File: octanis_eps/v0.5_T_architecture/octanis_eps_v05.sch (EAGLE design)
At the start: 141 parts, among them IC1 OPA2333DGK, Q3 32.768kHz, Q4 BSS123, U1 BQ24650_RVA_16, U10 CSD16327Q3_DQG_8, U13 CSD16327Q3_DQG_8, U14 CSD16327Q3_DQG_8, U2 TPS630250, U3 TPS630250, U4 TPS630250, U5 TPS2022D, U6 TPS61232, U7 CSD16327Q3_DQG_8, U8 MSP430G2544, U9 CSD16327Q3_DQG_8

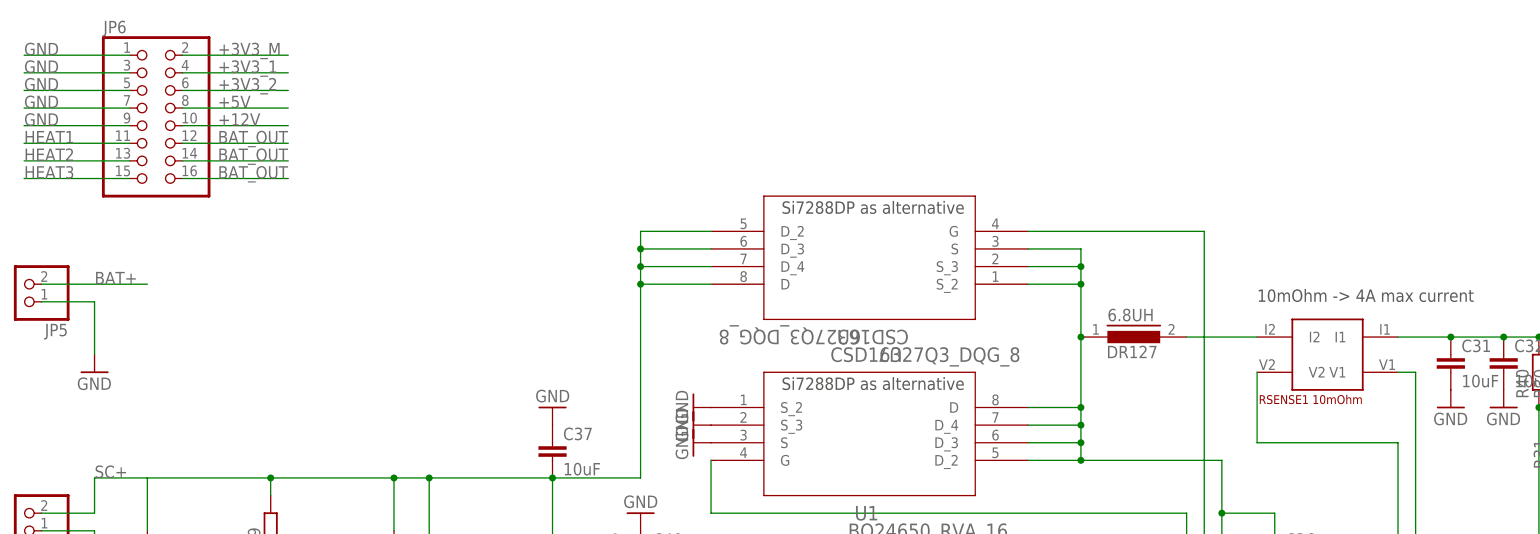
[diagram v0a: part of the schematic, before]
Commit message: Arranged parts for EPS v05
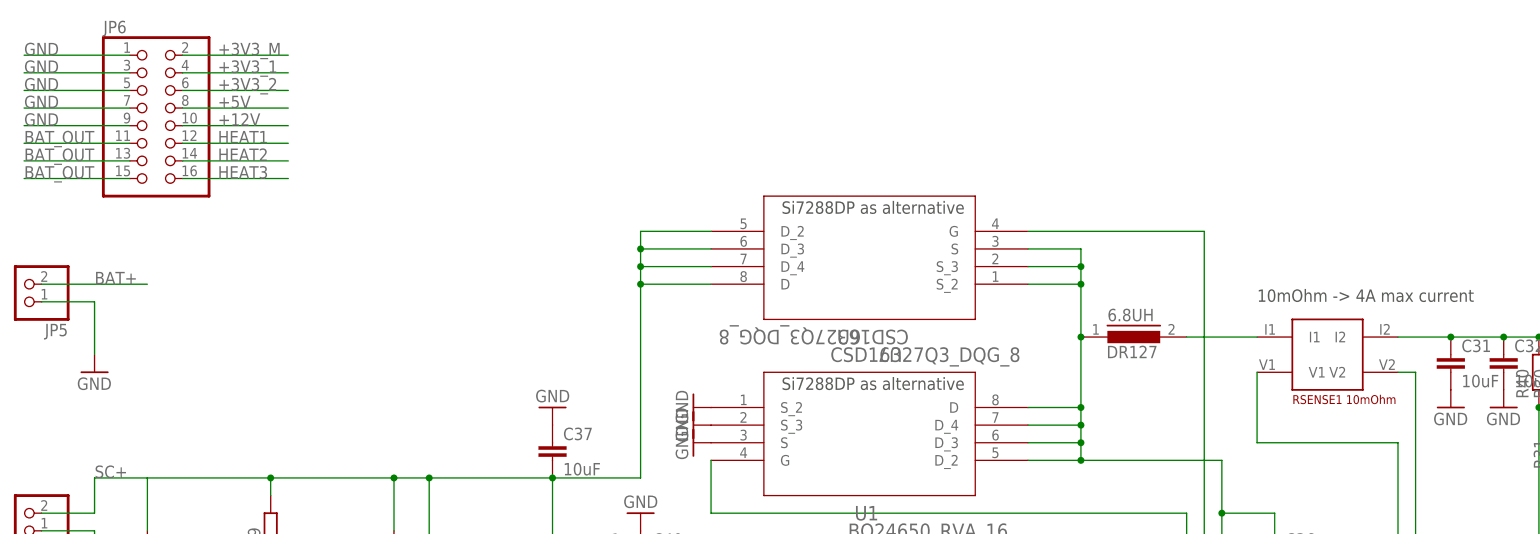
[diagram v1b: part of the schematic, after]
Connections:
- removed net N$79: 6.8UH.2, R_SENSE2.I2
- new net N$4: 6.8UH.2, R_SENSE2.I1
- net BAT_OUT: now also JP6.11, JP6.13, JP6.15; no longer JP6.12, JP6.14, JP6.16
- net HEAT1: now also JP6.12; no longer JP6.11
- net HEAT2: now also JP6.14; no longer JP6.13
- net HEAT3: now also JP6.16; no longer JP6.15
- net N$77: now also R_SENSE2.V1; no longer R_SENSE2.V2
- net N$78: now also R_SENSE2.V2; no longer R_SENSE2.V1
- net SC_OUT: now also R_SENSE2.I2; no longer R_SENSE2.I1
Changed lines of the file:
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@@
 <attribute name="VALUE" x="192.024" y="71.501" size="1.778" layer="96"/>
 </instance>
-<instance part="R_SENSE2" gate="G$1" x="193.04" y="101.6" rot="R180"/>
+<instance part="R_SENSE2" gate="G$1" x="203.2" y="101.6" rot="MR180"/>
 <instance part="GND57" gate="1" x="223.52" y="93.98"/>
 <instance part="GND58" gate="1" x="215.9" y="93.98"/>
@@
 </segment>
 <segment>
-<pinref part="JP6" gate="A" pin="15"/>
-<wire x1="25.4" y1="127" x2="10.16" y2="127" width="0.1524" layer="91"/>
-<label x="10.16" y="127" size="1.778" layer="95"/>
+<pinref part="JP6" gate="A" pin="16"/>
+<wire x1="33.02" y1="127" x2="48.26" y2="127" width="0.1524" layer="91"/>
+<label x="38.1" y="127" size="1.778" layer="95"/>
 </segment>
 </net>
@@
 </segment>
 <segment>
-<pinref part="JP6" gate="A" pin="13"/>
-<wire x1="25.4" y1="129.54" x2="10.16" y2="129.54" width="0.1524" layer="91"/>
-<label x="10.16" y="129.54" size="1.778" layer="95"/>
+<pinref part="JP6" gate="A" pin="14"/>
+<wire x1="33.02" y1="129.54" x2="48.26" y2="129.54" width="0.1524" layer="91"/>
+<label x="38.1" y="129.54" size="1.778" layer="95"/>
 </segment>
 </net>
@@
 </segment>
 <segment>
-<pinref part="JP6" gate="A" pin="11"/>
-<wire x1="25.4" y1="132.08" x2="10.16" y2="132.08" width="0.1524" layer="91"/>
-<label x="10.16" y="132.08" size="1.778" layer="95"/>
+<pinref part="JP6" gate="A" pin="12"/>
+<wire x1="33.02" y1="132.08" x2="48.26" y2="132.08" width="0.1524" layer="91"/>
+<label x="38.1" y="132.08" size="1.778" layer="95"/>
 </segment>
 </net>
@@
 <wire x1="182.88" y1="53.34" x2="208.28" y2="53.34" width="0.1524" layer="91"/>
 <wire x1="208.28" y1="53.34" x2="208.28" y2="88.9" width="0.1524" layer="91"/>
-<pinref part="R_SENSE2" gate="G$1" pin="V2"/>
 <wire x1="208.28" y1="88.9" x2="187.96" y2="88.9" width="0.1524" layer="91"/>
+<pinref part="R_SENSE2" gate="G$1" pin="V1"/>
 <wire x1="187.96" y1="88.9" x2="187.96" y2="99.06" width="0.1524" layer="91"/>
 </segment>
@@
 <wire x1="177.8" y1="45.72" x2="182.88" y2="45.72" width="0.1524" layer="91"/>
 <junction x="182.88" y="45.72"/>
-<pinref part="R_SENSE2" gate="G$1" pin="V1"/>
+<wire x1="210.82" y1="45.72" x2="182.88" y2="45.72" width="0.1524" layer="91"/>
+<pinref part="R_SENSE2" gate="G$1" pin="V2"/>
 <wire x1="208.28" y1="99.06" x2="210.82" y2="99.06" width="0.1524" layer="91"/>
 <wire x1="210.82" y1="99.06" x2="210.82" y2="45.72" width="0.1524" layer="91"/>
-<wire x1="210.82" y1="45.72" x2="182.88" y2="45.72" width="0.1524" layer="91"/>
 </segment>
 </net>
@@
 <wire x1="238.76" y1="101.6" x2="238.76" y2="104.14" width="0.1524" layer="91"/>
 <wire x1="238.76" y1="104.14" x2="231.14" y2="104.14" width="0.1524" layer="91"/>
-<pinref part="R_SENSE2" gate="G$1" pin="I1"/>
-<wire x1="208.28" y1="104.14" x2="215.9" y2="104.14" width="0.1524" layer="91"/>
 <pinref part="C31" gate="G$1" pin="1"/>
-<junction x="215.9" y="104.14"/>
 <wire x1="215.9" y1="104.14" x2="223.52" y2="104.14" width="0.1524" layer="91"/>
 <pinref part="C32" gate="G$1" pin="1"/>
@@
 <junction x="238.76" y="104.14"/>
 <label x="238.76" y="104.14" size="1.778" layer="95"/>
+<pinref part="R_SENSE2" gate="G$1" pin="I2"/>
+<wire x1="208.28" y1="104.14" x2="215.9" y2="104.14" width="0.1524" layer="91"/>
+<junction x="215.9" y="104.14"/>
 </segment>
 <segment>
@@
 <junction x="190.5" y="66.04"/>
 <pinref part="D1" gate="G$1" pin="CC"/>
-</segment>
-</net>
-<net name="N$79" class="0">
-<segment>
-<pinref part="6.8UH" gate="G$1" pin="2"/>
-<pinref part="R_SENSE2" gate="G$1" pin="I2"/>
-<wire x1="187.96" y1="104.14" x2="177.8" y2="104.14" width="0.1524" layer="91"/>
 </segment>
 </net>
@@
 </segment>
 <segment>
-<pinref part="JP6" gate="A" pin="12"/>
-<wire x1="33.02" y1="132.08" x2="48.26" y2="132.08" width="0.1524" layer="91"/>
-<label x="38.1" y="132.08" size="1.778" layer="95"/>
-</segment>
-<segment>
-<pinref part="JP6" gate="A" pin="14"/>
-<wire x1="33.02" y1="129.54" x2="48.26" y2="129.54" width="0.1524" layer="91"/>
-<label x="38.1" y="129.54" size="1.778" layer="95"/>
-</segment>
-<segment>
-<pinref part="JP6" gate="A" pin="16"/>
-<wire x1="33.02" y1="127" x2="48.26" y2="127" width="0.1524" layer="91"/>
-<label x="38.1" y="127" size="1.778" layer="95"/>
+<pinref part="JP6" gate="A" pin="11"/>
+<wire x1="25.4" y1="132.08" x2="10.16" y2="132.08" width="0.1524" layer="91"/>
+<label x="10.16" y="132.08" size="1.778" layer="95"/>
+</segment>
+<segment>
+<pinref part="JP6" gate="A" pin="13"/>
+<wire x1="25.4" y1="129.54" x2="10.16" y2="129.54" width="0.1524" layer="91"/>
+<label x="10.16" y="129.54" size="1.778" layer="95"/>
+</segment>
+<segment>
+<pinref part="JP6" gate="A" pin="15"/>
+<wire x1="25.4" y1="127" x2="10.16" y2="127" width="0.1524" layer="91"/>
+<label x="10.16" y="127" size="1.778" layer="95"/>
 </segment>
 </net>
@@
 </segment>
 </net>
+<net name="N$4" class="0">
+<segment>
+<pinref part="R_SENSE2" gate="G$1" pin="I1"/>
+<pinref part="6.8UH" gate="G$1" pin="2"/>
+<wire x1="187.96" y1="104.14" x2="177.8" y2="104.14" width="0.1524" layer="91"/>
+</segment>
+</net>

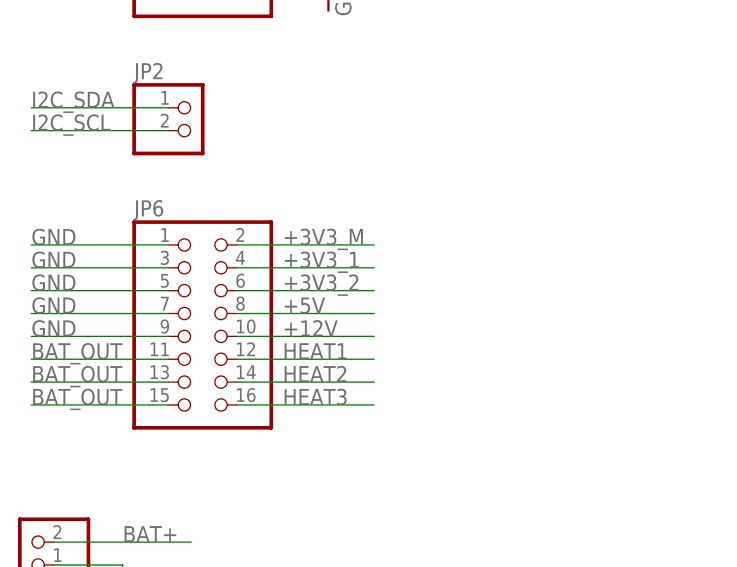
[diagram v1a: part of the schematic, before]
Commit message: Routed 3.3V, 5V and Solar Cell stepdown
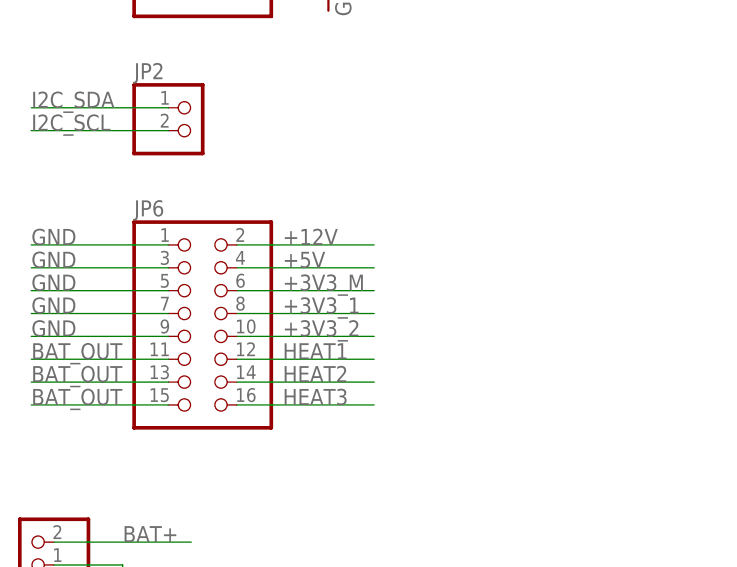
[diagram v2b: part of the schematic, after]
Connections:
- net +12V: now also JP6.2; no longer JP6.10
- net +3V3_1: now also JP6.8; no longer JP6.4
- net +3V3_2: now also JP6.10; no longer JP6.6
- net +3V3_M: now also JP6.6; no longer JP6.2
- net +5V: now also JP6.4; no longer JP6.8
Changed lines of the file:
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@@
 </segment>
 <segment>
-<pinref part="JP6" gate="A" pin="2"/>
-<wire x1="33.02" y1="144.78" x2="48.26" y2="144.78" width="0.1524" layer="91"/>
-<label x="38.1" y="144.78" size="1.778" layer="95"/>
+<pinref part="JP6" gate="A" pin="6"/>
+<wire x1="33.02" y1="139.7" x2="48.26" y2="139.7" width="0.1524" layer="91"/>
+<label x="38.1" y="139.7" size="1.778" layer="95"/>
 </segment>
 </net>
@@
 </segment>
 <segment>
-<pinref part="JP6" gate="A" pin="4"/>
-<wire x1="33.02" y1="142.24" x2="48.26" y2="142.24" width="0.1524" layer="91"/>
-<label x="38.1" y="142.24" size="1.778" layer="95"/>
+<pinref part="JP6" gate="A" pin="8"/>
+<wire x1="33.02" y1="137.16" x2="48.26" y2="137.16" width="0.1524" layer="91"/>
+<label x="38.1" y="137.16" size="1.778" layer="95"/>
 </segment>
 </net>
@@
 </segment>
 <segment>
-<pinref part="JP6" gate="A" pin="6"/>
-<wire x1="33.02" y1="139.7" x2="48.26" y2="139.7" width="0.1524" layer="91"/>
-<label x="38.1" y="139.7" size="1.778" layer="95"/>
+<pinref part="JP6" gate="A" pin="10"/>
+<wire x1="33.02" y1="134.62" x2="48.26" y2="134.62" width="0.1524" layer="91"/>
+<label x="38.1" y="134.62" size="1.778" layer="95"/>
 </segment>
 </net>
@@
 </segment>
 <segment>
-<pinref part="JP6" gate="A" pin="10"/>
-<wire x1="33.02" y1="134.62" x2="48.26" y2="134.62" width="0.1524" layer="91"/>
-<label x="38.1" y="134.62" size="1.778" layer="95"/>
+<pinref part="JP6" gate="A" pin="2"/>
+<wire x1="33.02" y1="144.78" x2="48.26" y2="144.78" width="0.1524" layer="91"/>
+<label x="38.1" y="144.78" size="1.778" layer="95"/>
 </segment>
 </net>
@@
 </segment>
 <segment>
-<pinref part="JP6" gate="A" pin="8"/>
-<wire x1="33.02" y1="137.16" x2="48.26" y2="137.16" width="0.1524" layer="91"/>
-<label x="38.1" y="137.16" size="1.778" layer="95"/>
-</segment>
-</net>
+<pinref part="JP6" gate="A" pin="4"/>
+<wire x1="33.02" y1="142.24" x2="48.26" y2="142.24" width="0.1524" layer="91"/>
+<label x="38.1" y="142.24" size="1.778" layer="95"/>
+</segment>
+</net>

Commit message: EPS v05 routing complete
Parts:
- U1: device texasinstruments:BQ24650_RVA_16 -> octanis_eps_v05:BQ24650_RVA_16
- U2, U3, U4: value TPS630250 -> Value; device texasinstruments:TPS630250RNCR -> octanis_eps_v05:TPS630250RNCR
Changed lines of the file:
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@@
 <classes>
 <class number="0" name="default" width="0" drill="0">
-<clearance class="0" value="0.205"/>
+<clearance class="0" value="0.1524"/>
 </class>
 <class number="1" name="power" width="0.2032" drill="0.3048">
@@
 </classes>
 <parts>
-<part name="U1" library="texasinstruments" deviceset="BQ24650_RVA_16" device=""/>
-<part name="U2" library="texasinstruments" deviceset="TPS630250RNCR" device="" value="TPS630250"/>
+<part name="U1" library="octanis_eps_v05" deviceset="BQ24650_RVA_16" device=""/>
+<part name="U2" library="octanis_eps_v05" deviceset="TPS630250RNCR" device="" value="Value"/>
 <part name="U5" library="Octanis1_EPS" deviceset="TPS2022D" device=""/>
 <part name="U8" library="Octanis1_EPS" deviceset="MSP430G2544" device=""/>
@@
 <part name="GND6" library="supply1" deviceset="GND" device=""/>
 <part name="GND7" library="supply1" deviceset="GND" device=""/>
-<part name="U3" library="texasinstruments" deviceset="TPS630250RNCR" device="" value="TPS630250"/>
+<part name="U3" library="octanis_eps_v05" deviceset="TPS630250RNCR" device="" value="Value"/>
 <part name="C4" library="resistor" deviceset="C-EU" device="C0805" value="10uF"/>
 <part name="C5" library="resistor" deviceset="C-EU" device="C0805" value="22uF"/>
@@
 <part name="GND8" library="supply1" deviceset="GND" device=""/>
 <part name="GND9" library="supply1" deviceset="GND" device=""/>
-<part name="U4" library="texasinstruments" deviceset="TPS630250RNCR" device="" value="TPS630250"/>
+<part name="U4" library="octanis_eps_v05" deviceset="TPS630250RNCR" device="" value="Value"/>
 <part name="C7" library="resistor" deviceset="C-EU" device="C0805" value="10uF"/>
 <part name="C8" library="resistor" deviceset="C-EU" device="C0805" value="22uF"/>

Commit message: Labels of EPS05 changed
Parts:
- removed C39: 1uF, rcl:C-EUC0603
- removed C40: 1u, rcl:C-EUC0603
- removed C42: 47uF Tantal, rcl:C-EUC1210
- removed L5: 1.5uH, Coilcraft:XFL4020
- removed R107, R116, R118: 200k, rcl:R-EU_R0603
- removed R108, R117, R119: 100k, rcl:R-EU_R0603
- removed U13, U14: CSD16327Q3_DQG_8, texasinstruments:CSD16327Q3_DQG_8
- added C100: 100nF, rcl:C-EUC0603
- added C101: 1uF, rcl:C-EUC0603
- added C104: 10uF, resistor:C-EUC0805
- added L100: 1uH, Coilcraft:XFL4020
- added R100, R101: (no value), rcl:R-EU_R0603
- added R102: 1M, rcl:R-EU_R0603
- added R36: 56k, resistor:R-EU_R0603
- added R37: 150-220k, resistor:R-EU_R0603
- added R38: 470k, resistor:R-EU_R0603
- added U100: Value, octanis_eps_v05:TPS630250RNCR
- added U11: CSD16327Q3_DQG_8, texasinstruments:CSD16327Q3_DQG_8
- C1: value 10uF -> 1.5uF; device resistor:C-EUC0805 -> rcl:C-EUC0603
- C10: value 22uF -> 10uF; device rcl:C-EUC0603 -> resistor:C-EUC0805
- C102: value 100nF -> 22uF; device rcl:C-EUC0603 -> resistor:C-EUC0805
- C103: value 10uF -> 22uF; device rcl:CPOL-EUA/3216-18R -> resistor:C-EUC0805
- C13: value 22uF -> 10nF; device resistor:C-EUC0805 -> rcl:C-EUC0603
- C14: value 10nF -> 10uF; device rcl:C-EUC0603 -> resistor:C-EUC0805
- C15: value 1.5uF -> 100nF
- C16, C17, C18: value 1.5uF -> 22uF; device rcl:C-EUC0603 -> resistor:C-EUC0805
- C19: value 100nF -> 22uF
- C2, C8, C9: value 22uF -> 1.5uF; device resistor:C-EUC0805 -> rcl:C-EUC0603
- C20: value 100nF -> 1uF
- C21: value 100nF -> 1u
- C23: value 47nF -> 2.2uF
- C26: value 22uF -> 22pF; device resistor:C-EUC0805 -> rcl:C-EUC0603
- C27: value 22uF -> 1uF; device resistor:C-EUC0805 -> rcl:C-EUC0603
- C29: value 1uF -> 22uF; device rcl:C-EUC0603 -> resistor:C-EUC0805
- C3: value 22uF -> 100nF; device resistor:C-EUC0805 -> rcl:C-EUC0603
- C30: value 10uF -> 22uF
- C31, C4: value 10uF -> 100nF; device resistor:C-EUC0805 -> rcl:C-EUC0603
- C33: value 1uF -> 47uF Tantal; device rcl:C-EUC0603 -> rcl:C-EUC1210
- C34: value 22pF -> 10uF; device rcl:C-EUC0603 -> resistor:C-EUC0805
- C36: value 100nF -> 47nF
- C38: value 2.2uF -> 10uF; device rcl:C-EUC0603 -> resistor:C-EUC0805
- C7: device resistor:C-EUC0805 -> rcl:CPOL-EUA/3216-18R
- JP1: device Headerlibrary:PINHD-1X2 -> Headerlibrary:PINHD-2X4
- JP3: device Headerlibrary:PINHD-2X4 -> Headerlibrary:PINHD-1X2
- JP4: device Headerlibrary:PINHD-1X2 -> Headerlibrary:PINHD-2X8
- JP6: device Headerlibrary:PINHD-2X8 -> Headerlibrary:PINHD-1X2
- L4: value 1uH -> 1.5uH
- R1, R2, R3: value 1M -> 1k; device resistor:R-EU_R0603 -> rcl:R-EU_R0603
- R10, R18: value 1k -> 200k
- R103: value 200k -> 1M
- R104: value 100k -> 1M; device rcl:R-EU_R0603 -> resistor:R-EU_R0603
- R11, R12, R7: value 1M -> 1k
- R15: value 1M -> 1.5k
- R16: value 1k -> 4.7k
- R17, R20, R9: value 1k -> 100k
- R19: value 1k -> 10k
- R21: value 4.7k -> 100k
- R22: value 47k -> 200k; device resistor:R-EU_R0603 -> rcl:R-EU_R0603
- R23: value 470k -> 200k; device resistor:R-EU_R0603 -> rcl:R-EU_R0603
- R24: value 56k -> 1M
- R25: value 270k -> 1k; device resistor:R-EU_R0603 -> rcl:R-EU_R0603
- R26: value 150-220k -> 1k; device resistor:R-EU_R0603 -> rcl:R-EU_R0603
- R27: value (none) -> 1M; device rcl:R-EU_R0603 -> resistor:R-EU_R0603
- R28: value (none) -> 1M
- R29: value 10 -> 4k7; device rcl:R-EU_R1206 -> rcl:R-EU_R0603
- R30: value 100k -> 1M
- R31: value 100k -> 4k7
- R32, R33: value 4k7 -> 100k
- R34: value 1M -> 2.2M
- R35: value 2 -> 270k; device rcl:R-EU_R2012 -> resistor:R-EU_R0603
- R39: value 1M -> 47k; device rcl:R-EU_R0603 -> resistor:R-EU_R0603
- R4: value 1k -> 1M
- R40: value 2.2M -> 10; device rcl:R-EU_R0603 -> rcl:R-EU_R1206
- R41: value 10k -> 2; device rcl:R-EU_R0603 -> rcl:R-EU_R2012
- R6: value 1.5k -> 1M
- R_SENSE1: value RSENSE1 -> RSENSE1 10mOhm
- R_SENSE2: value RSENSE1 10mOhm -> RSENSE1
- U1: value BQ24650_RVA_16 -> CSD16327Q3_DQG_8; device octanis_eps_v05:BQ24650_RVA_16 -> texasinstruments:CSD16327Q3_DQG_8
- U2, U3: value Value -> CSD16327Q3_DQG_8; device octanis_eps_v05:TPS630250RNCR -> texasinstruments:CSD16327Q3_DQG_8
- U4: value Value -> MSP430G2544; device octanis_eps_v05:TPS630250RNCR -> Octanis1_EPS:MSP430G2544
- U6: value TPS61232 -> Value; device texasinstruments:TPS61232 -> octanis_eps_v05:TPS630250RNCR
- U7: value CSD16327Q3_DQG_8 -> Value; device texasinstruments:CSD16327Q3_DQG_8 -> octanis_eps_v05:TPS630250RNCR
- U8: value MSP430G2544 -> TPS61232; device Octanis1_EPS:MSP430G2544 -> texasinstruments:TPS61232
- U9: value CSD16327Q3_DQG_8 -> BQ24650_RVA_16; device texasinstruments:CSD16327Q3_DQG_8 -> octanis_eps_v05:BQ24650_RVA_16
- renumbered LED1 to VCC, LED2 to +3V3_M, LED3 to +3V3_1, LED4 to +3V3_2, LED5 to +5V, LED6 to +11V, LED7 to STAT1, LED8 to STAT2, Q3 to Q1, Q4 to Q100
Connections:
- net +12V: now also C30.2, JP4.2, R38.2; no longer C26.2, JP6.2, R23.2
- net +3V3: now also C4.1, C5.1, C6.1, C7.+, R19.2, R24.2, U4.DVCC, U7.FB, U7.VOUT, U7.VOUT_2, U7.VOUT_3; no longer C102.1, C103.+, C2.1, C3.1, R1.2, R41.2, U2.FB, U2.VOUT, U2.VOUT_2, U2.VOUT_3, U8.DVCC
- net +3V3_1: now also C11.1, C12.1, JP4.8, U6.FB, U6.VOUT, U6.VOUT_2, U6.VOUT_3; no longer C5.1, C6.1, JP6.8, U3.FB, U3.VOUT, U3.VOUT_2, U3.VOUT_3
- net +3V3_2: now also C102.1, C103.1, JP4.10, U100.FB, U100.VOUT, U100.VOUT_2, U100.VOUT_3; no longer C8.1, C9.1, JP6.10, U4.FB, U4.VOUT, U4.VOUT_2, U4.VOUT_3
- net +3V3_M: now also JP4.6; no longer JP6.6
- net +5V: now also C16.1, C17.1, C18.1, JP4.4, R28.2, U8.FB, U8.VOUT; no longer C11.1, C12.1, C13.1, JP6.4, R8.2, U6.FB, U6.VOUT
- net A_EXT1: now also JP1.1, U4.P2.4/TA2/A4/VREF+/VEREF+; no longer JP3.1, U8.P2.4/TA2/A4/VREF+/VEREF+
- net A_EXT2: now also JP1.3, U4.P3.0/UCB0STE/UCA0CLK/A5; no longer JP3.3, U8.P3.0/UCB0STE/UCA0CLK/A5
- net A_EXT3: now also JP1.5, U4.P3.6/A6; no longer JP3.5, U8.P3.6/A6
- net A_EXT4: now also JP1.7, U4.P3.7/A7; no longer JP3.7, U8.P3.7/A7
- net BAT+: now also JP6.2, R23.2, R_SENSE2.I1; no longer JP5.2, R103.2, R_SENSE1.I1
- net BAT_OUT: now also C104.1, C14.1, C19.1, C33.1, C34.1, C35.1, JP4.11, JP4.13, JP4.15, L3.1, L4.1, R_SENSE2.I2, U100.VIN, U100.VINA, U100.VIN_2, U100.VIN_3, U6.VINA, U6.VIN_2, U6.VIN_3, U7.EN, U7.VIN, U7.VINA, U7.VIN_2, U7.VIN_3, U8.VIN; no longer C1.1, C21.1, C30.1, C4.1, C42.1, C7.1, JP6.11, JP6.13, JP6.15, L1.1, L5.1, R_SENSE1.I2, U2.EN, U2.VIN, U2.VINA, U2.VIN_2, U2.VIN_3, U3.VIN, U3.VINA, U3.VIN_2, U3.VIN_3, U4.VIN, U4.VINA, U4.VIN_2, U4.VIN_3
- net EN_12V: now also U4.P1.7/TA2/TDO/TDI; no longer U8.P1.7/TA2/TDO/TDI
- net EN_3V3_1: now also R27.1, U4.P1.4/SMCLK/TCK, U6.EN; no longer R2.1, U3.EN, U8.P1.4/SMCLK/TCK
- net EN_3V3_2: now also R104.1, U100.EN, U4.P1.5/TA0/TMS; no longer R3.1, U4.EN, U8.P1.5/TA0/TMS
- net EN_3V3_M: now also R24.1, U4.P1.3/TA2; no longer R1.1, U8.P1.3/TA2
- net EN_5V: now also R30.2, U4.P1.6/TA1/TDI, U8.EN; no longer R7.2, U6.EN, U8.P1.6/TA1/TDI
- net EN_HEAT1: now also R3.2, R4.1, U4.P1.0/TACLK/ADC10CLK; no longer R14.2, R15.1, U8.P1.0/TACLK/ADC10CLK
- net EN_HEAT2: now also R5.2, R6.1, U4.P1.1/TA0; no longer R10.2, R11.1, U8.P1.1/TA0
- net EN_HEAT3: now also R7.2, R8.1, U4.P1.2/TA1; no longer R12.1, R9.2, U8.P1.2/TA1
- net EN_SC: now also R102.1, R103.2, U4.P2.5/ROSC; no longer R34.2, R39.1, U8.P2.5/ROSC
- net GND: now also C1.1, C101.2, C103.2, C104.2, C16.2, C17.2, C18.2, C2.1, C20.2, C30.1, C32.1, C34.2, C35.2, C36.2, C37.2, C7.-, C8.1, C9.1, JP1.2, JP1.4, JP1.6, JP1.8, JP4.3, JP4.5, JP4.7, JP4.9, R10.2, R100.1, R103.1, R104.2, R18.2, R20.1, R21.1, R27.2, R30.1, R33.1, R35.1, R36.1, R4.2, R6.2, R8.2, U1.S, U1.S_2, U1.S_3, U100.GND, U100.PFM_PWM, U100.PGND, U11.S, U11.S_2, U11.S_3, U2.S, U2.S_2, U2.S_3, U3.S, U3.S_2, U3.S_3, U4.AVSS, U4.DVSS, U6.PFM_PWM, U6.PGND, U7.GND, U7.PFM_PWM, U7.PGND, U8.GND, U8.GND1, U8.GND2, U8.GND3, U8.GND4, U8.GND5, U9.EPAD, U9.GND, U9.TERM_EN; no longer C1.2, C103.-, C15.1, C16.1, C17.1, C18.1, C2.2, C26.1, C30.2, C31.2, C32.2, C37.1, C39.2, C40.2, C42.2, C7.2, C8.2, C9.2, JP3.2, JP3.4, JP3.6, JP3.8, JP6.3, JP6.5, JP6.7, JP6.9, R104.1, R107.2, R11.2, R117.1, R118.2, R12.2, R15.2, R2.2, R24.1, R25.1, R28.1, R3.2, R31.1, R34.1, R7.1, U1.EPAD, U1.GND, U1.TERM_EN, U10.S, U10.S_2, U10.S_3, U13.S, U13.S_2, U13.S_3, U14.S, U14.S_2, U14.S_3, U2.GND, U2.PFM_PWM, U2.PGND, U3.GND, U3.PFM_PWM, U3.PGND, U4.GND, U4.PFM_PWM, U4.PGND, U6.GND1, U6.GND2, U6.GND3, U6.GND4, U6.GND5, U8.AVSS, U8.DVSS, U9.S, U9.S_2, U9.S_3
- net HEAT1: now also JP4.12, U1.D, U1.D_2, U1.D_3, U1.D_4; no longer JP6.12, U14.D, U14.D_2, U14.D_3, U14.D_4
- net HEAT2: now also JP4.14, U2.D, U2.D_2, U2.D_3, U2.D_4; no longer JP6.14, U10.D, U10.D_2, U10.D_3, U10.D_4
- net HEAT3: now also JP4.16, U3.D, U3.D_2, U3.D_3, U3.D_4; no longer JP6.16, U13.D, U13.D_2, U13.D_3, U13.D_4
- net I2C_SCL: now also JP3.2, U4.P3.2/UCB0SOMI/UCB0SCL; no longer JP2.2, U8.P3.2/UCB0SOMI/UCB0SCL
- net I2C_SDA: now also JP3.1, U4.P3.1/UCB0SIMO/UCB0SDA; no longer JP2.1, U8.P3.1/UCB0SIMO/UCB0SDA
- net IND: now also L3.2, U8.SW; no longer L1.2, U6.SW
- net I_IN: now also C8.2, R25.1, U4.P2.1/TAINCLK/SMCLK/A1; no longer C18.2, R5.1, U8.P2.1/TAINCLK/SMCLK/A1
- net I_OUT: now also C9.2, R26.1, U4.P2.0/ACLK/A0; no longer C17.2, R4.1, U8.P2.0/ACLK/A0
- net LED5: now also R15.2; no longer R6.2
- net N$1: now also U7.L1; no longer U2.L1
- net N$11: now also L100.1, U100.L1; no longer L4.1, U4.L1
- net N$12: now also L100.2, U100.L2; no longer L4.2, U4.L2
- net N$14: now also R15.1; no longer R6.1
- net N$19: now also R1.2, R9.1; no longer R108.1, R17.2
- net N$2: now also R28.1, U8.PG; no longer R8.1, U6.PG
- net N$20: now also R10.1, R9.2; no longer R107.1, R108.2
- net N$21: now also R21.2, R23.1; no longer R103.1, R104.2
- net N$22: now also R17.1, R2.2; no longer R119.1, R13.2
- net N$23: now also R17.2, R18.1; no longer R118.1, R119.2
- net N$24: now also R20.2, R22.1; no longer R116.1, R117.2
- net N$25: now also R26.2; no longer R4.2
- net N$26: now also R25.2; no longer R5.2
- net N$27: now also R7.1, U3.G; no longer R9.1, U13.G
- net N$3: now also U7.L2; no longer U2.L2
- net N$30: now also U4.XIN/P2.6; no longer U8.XIN/P2.6
- net N$31: now also R5.1, U2.G; no longer R10.1, U10.G
- net N$32: now also R_SENSE2.V1; no longer R_SENSE1.V1
- net N$33: now also R_SENSE2.V2; no longer R_SENSE1.V2
- net N$36: now also U4.XOUT/P2.7; no longer U8.XOUT/P2.7
- net N$37: now also R3.1, U1.G; no longer R14.1, U14.G
- net N$38: now also C31.2; no longer C20.2
- net N$39: now also R12.2; no longer R16.2
- net N$4: now also R_SENSE1.I1; no longer R_SENSE2.I1
- net N$40: now also R12.1; no longer R16.1
- net N$43: now also R11.2; no longer R18.2
- net N$45: now also R11.1; no longer R18.1
- net N$46: now also R14.2; no longer R20.2
- net N$47: now also R14.1; no longer R20.1
- net N$48: now also R16.2; no longer R21.2
- net N$49: now also R16.1; no longer R21.1
- net N$5: now also C13.1, U8.SS; no longer C14.1, U6.SS
- net N$50: now also C31.1, L4.2, R39.2; no longer C20.1, L5.2, R22.2
- net N$51: now also R13.2; no longer R19.2
- net N$52: now also R13.1; no longer R19.1
- net N$53: now also R39.1; no longer R22.1
- net N$54: now also R37.1; no longer R26.1
- net N$56: now also C36.1; no longer C23.1
- net N$57: now also R35.2; no longer R25.2
- net N$58: now also R37.2; no longer R26.2
- net N$59: now also C23.1; no longer C22.1
- net N$6: now also L1.1, U6.L1; no longer L3.1, U3.L1
- net N$60: now also R36.2, R38.1; no longer R23.1, R24.2
- net N$64: now also R100.2, R101.1, U9.MPPSET; no longer R27.1, R28.2, U1.MPPSET
- net N$65: now also C22.1, R41.1; no longer C38.1, R35.1
- net N$66: now also R31.1; no longer R33.1
- net N$67: now also J7.2; no longer J8.2
- net N$68: now also J8.2; no longer J7.2
- net N$69: now also R29.1; no longer R32.1
- net N$7: now also L1.2, U6.L2; no longer L3.2, U3.L2
- net N$70: now also J7.1, U9.STAT2; no longer J8.1, U1.STAT2
- net N$71: now also J8.1, U9.STAT1; no longer J7.1, U1.STAT1
- net N$72: now also C20.1, U9.VREF; no longer C39.1, U1.VREF
- net N$73: now also C21.1, R40.2, U9.VCC; no longer C40.1, R29.2, U1.VCC
- net N$75: now also JP2.2, U4.TEST/SBWTCK; no longer JP1.2, U8.TEST/SBWTCK
- net N$76: now also C100.1, U10.S, U10.S_2, U10.S_3, U11.D, U11.D_2, U11.D_3, U11.D_4, U9.PH; no longer C36.1, U1.PH, U7.S, U7.S_2, U7.S_3, U9.D, U9.D_2, U9.D_3, U9.D_4
- net N$77: now also C15.2, R_SENSE1.V1, U9.SRP; no longer C35.2, R_SENSE2.V1, U1.SRP
- net N$78: now also C15.1, R_SENSE1.V2, U9.SRN; no longer C35.1, R_SENSE2.V2, U1.SRN
- net N$80: now also U10.G, U9.HIDRV; no longer U1.HIDRV, U7.G
- net N$81: now also U11.G, U9.LODRV; no longer U1.LODRV, U9.G
- net N$82: now also C26.2, R32.1, R33.2, R34.1, U9.VFB; no longer C34.2, R30.1, R31.2, R40.1, U1.VFB
- net N$84: now also C101.1, U9.REGN; no longer C33.1, U1.REGN
- net N$85: now also C100.2, U9.BTST; no longer C36.2, U1.BTST
- net N$93: now also JP2.1, R19.1, U4.RST/NMI/SBWTDIO; no longer JP1.1, R41.1, U8.RST/NMI/SBWTDIO
- net N$99: now also C3.1, U4.AVCC; no longer C19.1, U8.AVCC
- net SC+: now also C32.2, JP5.2, R101.2, R102.2, R22.2, R29.2, R31.2, R40.1, R41.2, U10.D, U10.D_2, U10.D_3, U10.D_4; no longer C37.2, JP4.2, R116.2, R27.2, R29.1, R32.2, R33.2, R35.2, R39.2, U7.D, U7.D_2, U7.D_3, U7.D_4
- net SC_OUT: now also C26.1, C37.1, C38.1, R32.2, R34.2, R_SENSE1.I2; no longer C31.1, C32.1, C34.1, R30.2, R40.2, R_SENSE2.I2
- net V_BAT: now also C1.2, R1.1, U4.P2.3/TA1/A3/VREF−/VEREF-; no longer C15.2, R17.1, U8.P2.3/TA1/A3/VREF−/VEREF-
- net V_SC: now also C2.2, R2.1, U4.P2.2/TA0/A2; no longer C16.2, R13.1, U8.P2.2/TA0/A2
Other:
- moved on the sheet: C1, C10, C102, C11, C12, C13, C14, C15, C16, C17, C18, C19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
